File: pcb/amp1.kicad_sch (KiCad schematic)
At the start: 15 parts, among them Q1 BFP640, U1 Single_Stub_Input, U2 Single_Stub_Output

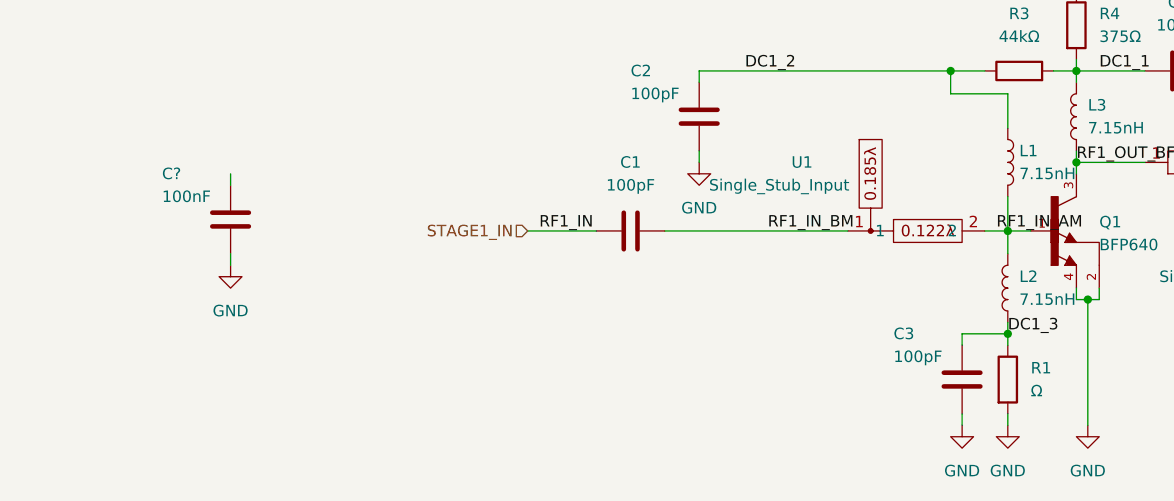
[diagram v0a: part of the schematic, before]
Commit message: alternate board
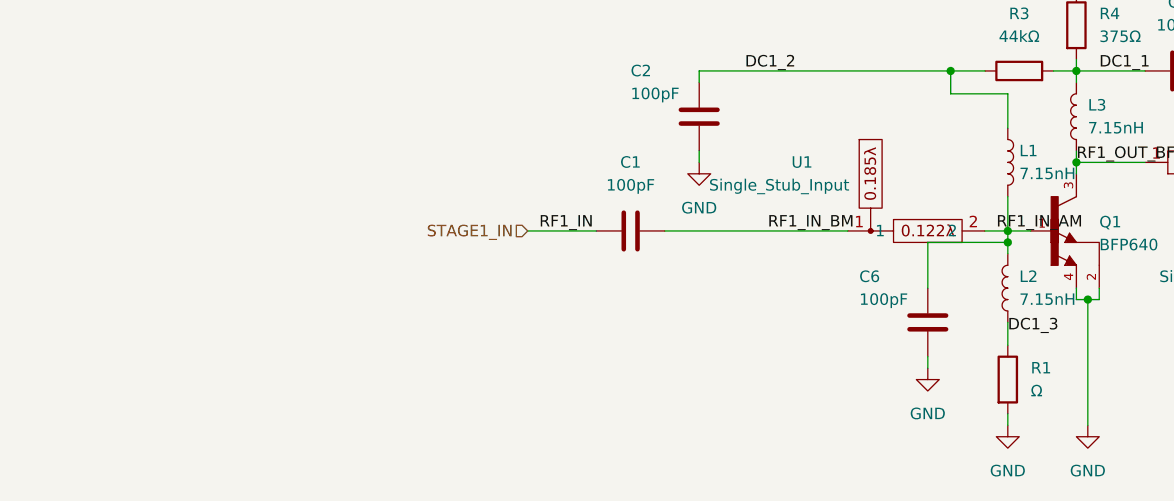
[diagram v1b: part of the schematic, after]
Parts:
- removed C3: 100pF, Capacitor_SMD:C_0603_1608Metric, symbol Device:C
- removed C?: 100nF, Capacitor_SMD:C_1206_3216Metric, symbol Device:C
- added C6: 100pF, Capacitor_SMD:C_0603_1608Metric, symbol Device:C
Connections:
- net GND: now also C6.2
- net RF1_IN_AM: now also C6.1
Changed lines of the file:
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@@
   (junction (at 153.67 88.9) (diameter 0) (color 0 0 0 0)
   )
-  (junction (at 146.05 118.11) (diameter 0) (color 0 0 0 0)
+  (junction (at 146.05 107.95) (diameter 0) (color 0 0 0 0)
   )
   (junction (at 153.67 99.06) (diameter 0) (color 0 0 0 0)
@@
     (stroke (width 0) (type default) (color 0 0 0 0))
   )
+  (wire (pts (xy 137.16 120.65) (xy 137.16 121.92))
+    (stroke (width 0) (type default) (color 0 0 0 0))
+  )
   (wire (pts (xy 153.67 99.06) (xy 161.29 99.06))
     (stroke (width 0) (type default) (color 0 0 0 0))
@@
     (stroke (width 0) (type default) (color 0 0 0 0))
   )
-  (wire (pts (xy 146.05 116.84) (xy 146.05 118.11))
+  (wire (pts (xy 146.05 107.95) (xy 146.05 109.22))
+    (stroke (width 0) (type default) (color 0 0 0 0))
+  )
+  (wire (pts (xy 146.05 116.84) (xy 146.05 119.38))
     (stroke (width 0) (type default) (color 0 0 0 0))
   )
@@
     (stroke (width 0) (type default) (color 0 0 0 0))
   )
-  (wire (pts (xy 59.69 109.22) (xy 59.69 110.49))
-    (stroke (width 0) (type default) (color 0 0 0 0))
-  )
   (wire (pts (xy 154.94 114.3) (xy 153.67 114.3))
     (stroke (width 0) (type default) (color 0 0 0 0))
@@
     (stroke (width 0) (type default) (color 0 0 0 0))
   )
-  (wire (pts (xy 140.97 127) (xy 140.97 128.27))
-    (stroke (width 0) (type default) (color 0 0 0 0))
-  )
   (wire (pts (xy 146.05 91.44) (xy 139.7 91.44))
     (stroke (width 0) (type default) (color 0 0 0 0))
@@
     (stroke (width 0) (type default) (color 0 0 0 0))
   )
-  (wire (pts (xy 140.97 118.11) (xy 146.05 118.11))
-    (stroke (width 0) (type default) (color 0 0 0 0))
-  )
   (wire (pts (xy 151.13 88.9) (xy 153.67 88.9))
     (stroke (width 0) (type default) (color 0 0 0 0))
@@
     (stroke (width 0) (type default) (color 0 0 0 0))
   )
-  (wire (pts (xy 140.97 119.38) (xy 140.97 118.11))
-    (stroke (width 0) (type default) (color 0 0 0 0))
-  )
   (wire (pts (xy 143.51 106.68) (xy 146.05 106.68))
     (stroke (width 0) (type default) (color 0 0 0 0))
@@
     (stroke (width 0) (type default) (color 0 0 0 0))
   )
-  (wire (pts (xy 59.69 101.6) (xy 59.69 100.33))
+  (wire (pts (xy 137.16 113.03) (xy 137.16 107.95))
+    (stroke (width 0) (type default) (color 0 0 0 0))
+  )
+  (wire (pts (xy 146.05 106.68) (xy 146.05 107.95))
     (stroke (width 0) (type default) (color 0 0 0 0))
   )
@@
     (stroke (width 0) (type default) (color 0 0 0 0))
   )
-  (wire (pts (xy 146.05 118.11) (xy 146.05 119.38))
-    (stroke (width 0) (type default) (color 0 0 0 0))
-  )
   (wire (pts (xy 139.7 88.9) (xy 143.51 88.9))
     (stroke (width 0) (type default) (color 0 0 0 0))
@@
     (stroke (width 0) (type default) (color 0 0 0 0))
   )
+  (wire (pts (xy 137.16 107.95) (xy 146.05 107.95))
+    (stroke (width 0) (type default) (color 0 0 0 0))
+  )
   (wire (pts (xy 146.05 127) (xy 146.05 128.27))
-    (stroke (width 0) (type default) (color 0 0 0 0))
-  )
-  (wire (pts (xy 146.05 109.22) (xy 146.05 106.68))
     (stroke (width 0) (type default) (color 0 0 0 0))
   )
@@
   (hierarchical_label "VCC" (shape input) (at 153.67 77.47 90)
     (effects (font (size 1.27 1.27)) (justify left))
-  )
-  (symbol (lib_id "Device:C") (at 59.69 105.41 0) (mirror y) (unit 1)
-    (in_bom yes) (on_board yes)
-    (property "Reference" "C?" (id 0) (at 52.07 100.33 0)
-      (effects (font (size 1.27 1.27)) (justify right))
-    )
-    (property "Value" "100nF" (id 1) (at 52.07 102.87 0)
-      (effects (font (size 1.27 1.27)) (justify right))
-    )
-    (property "Footprint" "Capacitor_SMD:C_1206_3216Metric" (id 2) (at 58.7248 109.22 0)
-      (effects (font (size 1.27 1.27)) hide)
-    )
-    (property "Datasheet" "~" (id 3) (at 59.69 105.41 0)
-      (effects (font (size 1.27 1.27)) hide)
-    )
-    (pin "1")
-    (pin "2")
   )
   (symbol (lib_id "Device:C") (at 111.76 93.98 0) (mirror y) (unit 1)
@@
     (pin "2")
   )
+  (symbol (lib_id "power:GND") (at 137.16 121.92 0) (unit 1)
+    (in_bom yes) (on_board yes) (fields_autoplaced)
+    (property "Reference" "#PWR0111" (id 0) (at 137.16 128.27 0)
+      (effects (font (size 1.27 1.27)) hide)
+    )
+    (property "Value" "GND" (id 1) (at 137.16 127 0))
+    (property "Footprint" "" (id 2) (at 137.16 121.92 0)
+      (effects (font (size 1.27 1.27)) hide)
+    )
+    (property "Datasheet" "" (id 3) (at 137.16 121.92 0)
+      (effects (font (size 1.27 1.27)) hide)
+    )
+    (pin "1")
+  )
   (symbol (lib_id "Device:R") (at 147.32 88.9 90) (unit 1)
     (in_bom yes) (on_board yes) (fields_autoplaced)
@@
     (pin "2")
   )
+  (symbol (lib_id "Device:C") (at 137.16 116.84 0) (mirror y) (unit 1)
+    (in_bom yes) (on_board yes)
+    (property "Reference" "C6" (id 0) (at 129.54 111.76 0)
+      (effects (font (size 1.27 1.27)) (justify right))
+    )
+    (property "Value" "100pF" (id 1) (at 129.54 114.3 0)
+      (effects (font (size 1.27 1.27)) (justify right))
+    )
+    (property "Footprint" "Capacitor_SMD:C_0603_1608Metric" (id 2) (at 136.1948 120.65 0)
+      (effects (font (size 1.27 1.27)) hide)
+    )
+    (property "Datasheet" "~" (id 3) (at 137.16 116.84 0)
+      (effects (font (size 1.27 1.27)) hide)
+    )
+    (pin "1")
+    (pin "2")
+  )
   (symbol (lib_id "power:GND") (at 170.18 91.44 0) (unit 1)
     (in_bom yes) (on_board yes)
@@
     )
     (property "Datasheet" "" (id 3) (at 170.18 91.44 0)
-      (effects (font (size 1.27 1.27)) hide)
-    )
-    (pin "1")
-  )
-  (symbol (lib_id "power:GND") (at 140.97 128.27 0) (unit 1)
-    (in_bom yes) (on_board yes) (fields_autoplaced)
-    (property "Reference" "#PWR0102" (id 0) (at 140.97 134.62 0)
-      (effects (font (size 1.27 1.27)) hide)
-    )
-    (property "Value" "GND" (id 1) (at 140.97 133.35 0))
-    (property "Footprint" "" (id 2) (at 140.97 128.27 0)
-      (effects (font (size 1.27 1.27)) hide)
-    )
-    (property "Datasheet" "" (id 3) (at 140.97 128.27 0)
       (effects (font (size 1.27 1.27)) hide)
     )
@@
     (pin "1")
   )
-  (symbol (lib_id "Device:C") (at 140.97 123.19 0) (mirror y) (unit 1)
-    (in_bom yes) (on_board yes)
-    (property "Reference" "C3" (id 0) (at 133.35 118.11 0)
-      (effects (font (size 1.27 1.27)) (justify right))
-    )
-    (property "Value" "100pF" (id 1) (at 133.35 120.65 0)
-      (effects (font (size 1.27 1.27)) (justify right))
-    )
-    (property "Footprint" "Capacitor_SMD:C_0603_1608Metric" (id 2) (at 140.0048 127 0)
-      (effects (font (size 1.27 1.27)) hide)
-    )
-    (property "Datasheet" "~" (id 3) (at 140.97 123.19 0)
-      (effects (font (size 1.27 1.27)) hide)
-    )
-    (pin "1")
-    (pin "2")
-  )
   (symbol (lib_id "power:GND") (at 154.94 128.27 0) (unit 1)
     (in_bom yes) (on_board yes) (fields_autoplaced)
@@
     (pin "2")
   )
-  (symbol (lib_id "power:GND") (at 59.69 110.49 0) (unit 1)
-    (in_bom yes) (on_board yes) (fields_autoplaced)
-    (property "Reference" "#PWR?" (id 0) (at 59.69 116.84 0)
-      (effects (font (size 1.27 1.27)) hide)
-    )
-    (property "Value" "GND" (id 1) (at 59.69 115.57 0))
-    (property "Footprint" "" (id 2) (at 59.69 110.49 0)
-      (effects (font (size 1.27 1.27)) hide)
-    )
-    (property "Datasheet" "" (id 3) (at 59.69 110.49 0)
-      (effects (font (size 1.27 1.27)) hide)
-    )
-    (pin "1")
-  )
   (symbol (lib_id "power:GND") (at 111.76 99.06 0) (unit 1)
